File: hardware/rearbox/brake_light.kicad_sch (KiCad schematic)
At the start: 4 parts, among them Q1 BUK6D210

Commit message: Changed power section
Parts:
- gave numbers to parts that had none: 2
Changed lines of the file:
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@@
 (kicad_sch
-	(version 20231120)
+	(version 20250114)
 	(generator "eeschema")
-	(generator_version "8.0")
+	(generator_version "9.0")
 	(paper "A4")
 	(title_block
@@
 		(comment 1 "Reviewer:")
 	)
+	(text "Brake Light"
+		(exclude_from_sim no)
+		(at 169.545 94.996 90)
+		(effects
+			(font
+				(size 1.27 1.27)
+			)
+			(justify left bottom)
+		)
+	)
+	(text "+24V"
+		(exclude_from_sim no)
+		(at 166.2684 77.1144 0)
+		(effects
+			(font
+				(size 1.27 1.27)
+			)
+			(justify left bottom)
+		)
+	)
 	(junction
 		(at 152.4 113.03)
@@
 		)
 	)
-	(text "Brake Light"
-		(exclude_from_sim no)
-		(at 169.545 94.996 90)
+	(hierarchical_label "OUT"
+		(shape output)
+		(at 156.21 97.79 0)
 		(effects
 			(font
 				(size 1.27 1.27)
 			)
-			(justify left bottom)
-		)
-	)
-	(text "+24V"
-		(exclude_from_sim no)
-		(at 166.2684 77.1144 0)
-		(effects
-			(font
-				(size 1.27 1.27)
-			)
-			(justify left bottom)
-		)
-	)
-	(hierarchical_label "OUT"
-		(shape output)
-		(at 156.21 97.79 0)
-		(fields_autoplaced yes)
-		(effects
-			(font
-				(size 1.27 1.27)
-			)
 			(justify left)
 		)
@@
 		(shape input)
 		(at 132.08 105.41 180)
-		(fields_autoplaced yes)
 		(effects
 			(font
@@
 		(on_board yes)
 		(dnp no)
-		(property "Reference" "R?"
+		(property "Reference" "R10"
 			(at 147.32 110.49 90)
 			(effects
@@
 		(on_board yes)
 		(dnp no)
-		(property "Reference" "R?"
+		(property "Reference" "R9"
 			(at 137.16 102.87 90)
 			(effects

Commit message: Sync :(
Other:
- note added: "30.07.2025 Currently ASSI B Q4 used as brake light transtor bo się spaliło :("
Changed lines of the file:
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@@
 		(comment 1 "Reviewer:")
+	)
+	(text "30.07.2025\nCurrently ASSI B Q4 used as brake light transtor\nbo się spaliło :(\n"
+		(exclude_from_sim no)
+		(at 129.032 91.694 0)
+		(effects
+			(font
+				(size 1.27 1.27)
+			)
+		)
 	)
 	(text "Brake Light"

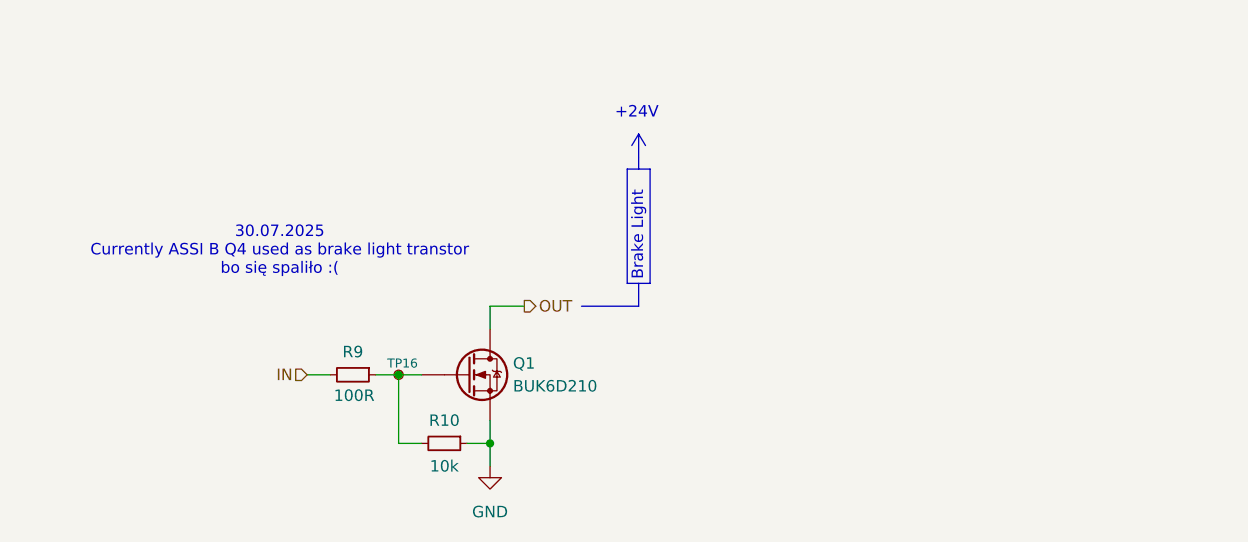
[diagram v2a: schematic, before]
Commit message: Added an auxillary transistor for rear brakelights in case they burn up again and fixed some GNDISO_CAN problems
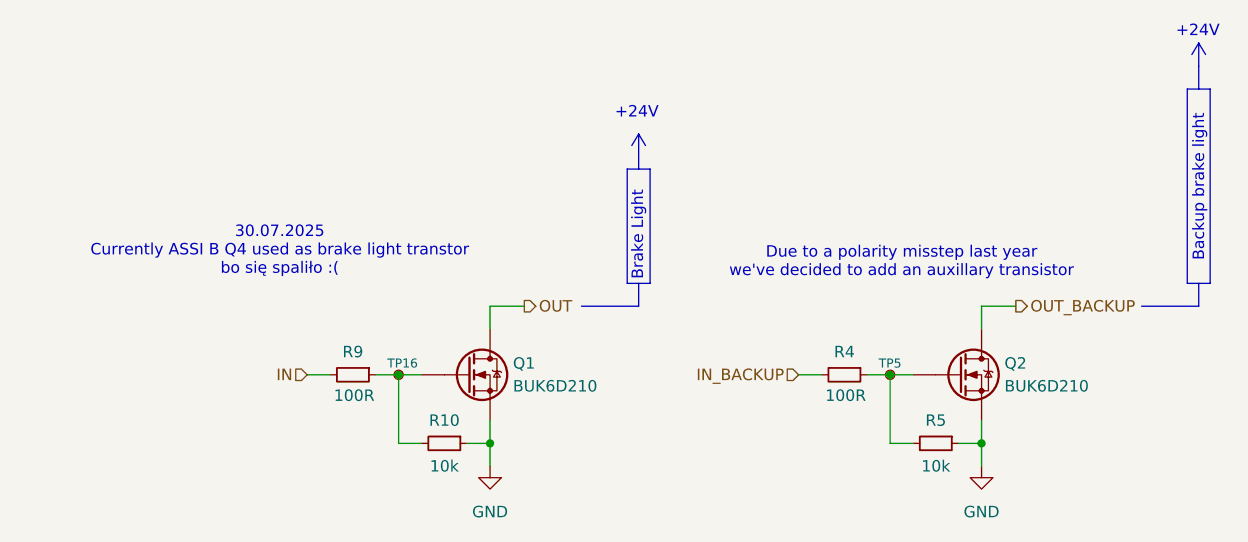
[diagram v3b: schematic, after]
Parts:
- added Q2: BUK6D210, Local_Library:Diodes_UDFN2020-6_Type-F, symbol BUK6D210:BUK6D210
- added R4: 100R, Resistor_SMD:R_0603_1608Metric, symbol Device:R_Small
- added R5: 10k, Resistor_SMD:R_0603_1608Metric, symbol Device:R_Small
- added TP5: TestPoint_Small, TestPoint:TestPoint_Pad_D1.0mm, symbol Connector:TestPoint_Small
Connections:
- net GND: now also Q2.4 (S), Q2.8 (S), R5.1
- new net: Q2.3 (G), R4.1, R5.2, TP5.1
- new net IN_BACKUP: R4.2
- new net OUT_BACKUP: Q2.1 (D), Q2.2 (D), Q2.5 (D), Q2.6 (D), Q2.7 (D)
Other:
- note added: "Due to a polarity misstep last year we've decided to add an auxillary transistor"
